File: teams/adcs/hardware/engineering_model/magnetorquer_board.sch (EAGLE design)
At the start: 35 parts

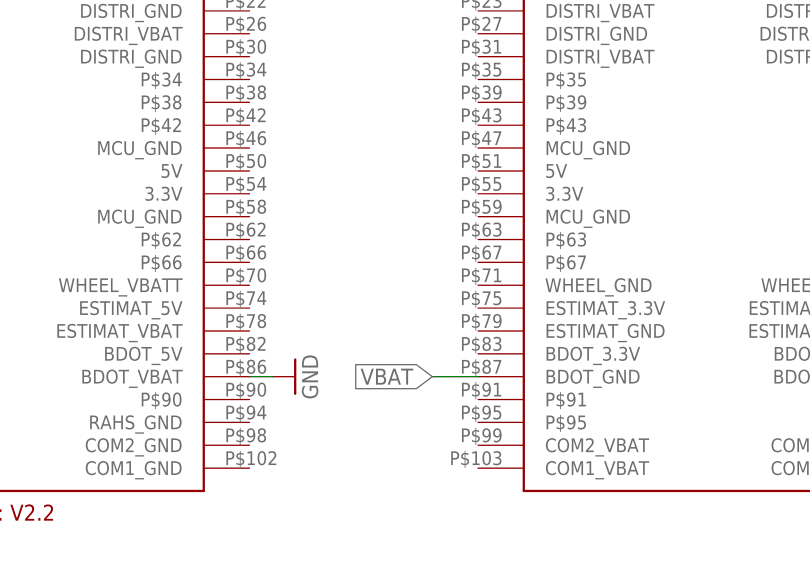
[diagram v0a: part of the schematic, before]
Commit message: ADCS/MT: Add capacitor to VBAT
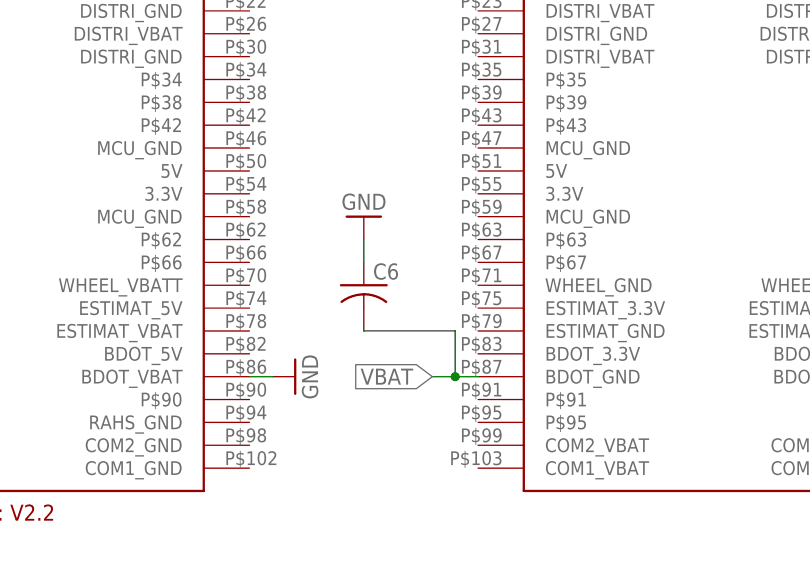
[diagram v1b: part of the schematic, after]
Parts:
- added C6: (no value), rcl:C-USC0805
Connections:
- net GND: now also C6.1
- net VBAT: now also C6.2
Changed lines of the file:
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@@
 <?xml version="1.0" encoding="utf-8"?>
 <!DOCTYPE eagle SYSTEM "eagle.dtd">
-<eagle version="8.3.2">
+<eagle version="8.4.0">
 <drawing>
 <settings>
@@
 <part name="R6" library="rcl" library_urn="urn:adsk.eagle:library:334" deviceset="R-US_" device="R0805" package3d_urn="urn:adsk.eagle:package:23553/2"/>
 <part name="GND21" library="supply1" library_urn="urn:adsk.eagle:library:371" deviceset="GND" device=""/>
+<part name="C6" library="rcl" library_urn="urn:adsk.eagle:library:334" deviceset="C-US" device="C0805" package3d_urn="urn:adsk.eagle:package:23617/2"/>
+<part name="GND23" library="supply1" library_urn="urn:adsk.eagle:library:371" deviceset="GND" device=""/>
 </parts>
 <sheets>
@@
 <instance part="R6" gate="G$1" x="58.42" y="147.32" rot="R90"/>
 <instance part="GND21" gate="1" x="58.42" y="139.7" rot="MR0"/>
+<instance part="C6" gate="G$1" x="43.18" y="43.18"/>
+<instance part="GND23" gate="1" x="43.18" y="50.8" rot="R180"/>
 </instances>
 <busses>
@@
 <pinref part="R6" gate="G$1" pin="1"/>
 <pinref part="GND21" gate="1" pin="GND"/>
+</segment>
+<segment>
+<pinref part="C6" gate="G$1" pin="1"/>
+<pinref part="GND23" gate="1" pin="GND"/>
+<wire x1="43.18" y1="45.72" x2="43.18" y2="48.26" width="0.1524" layer="91"/>
 </segment>
 </net>
@@
 <segment>
 <pinref part="U$1" gate="G$1" pin="BDOT_GND@87"/>
-<wire x1="55.88" y1="33.02" x2="50.8" y2="33.02" width="0.1524" layer="91"/>
+<wire x1="55.88" y1="33.02" x2="53.34" y2="33.02" width="0.1524" layer="91"/>
 <label x="50.8" y="33.02" size="1.778" layer="95" rot="R180" xref="yes"/>
-</segment>
-<segment>
+<pinref part="C6" gate="G$1" pin="2"/>
+<wire x1="53.34" y1="33.02" x2="50.8" y2="33.02" width="0.1524" layer="91"/>
+<wire x1="43.18" y1="38.1" x2="53.34" y2="38.1" width="0.1524" layer="91"/>
+<wire x1="53.34" y1="38.1" x2="53.34" y2="33.02" width="0.1524" layer="91"/>
+<junction x="53.34" y="33.02"/>
+</segment>
+<segment>

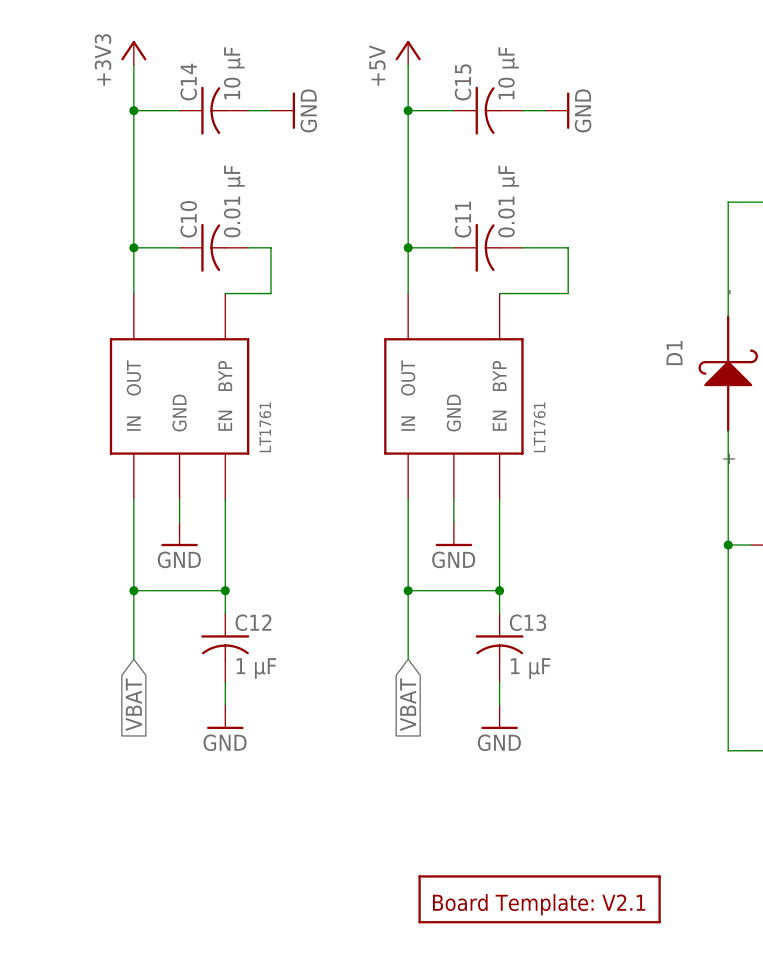
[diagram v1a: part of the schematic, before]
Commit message: ADCS/MT: Switched existing LDOs to LDOs from design blocks
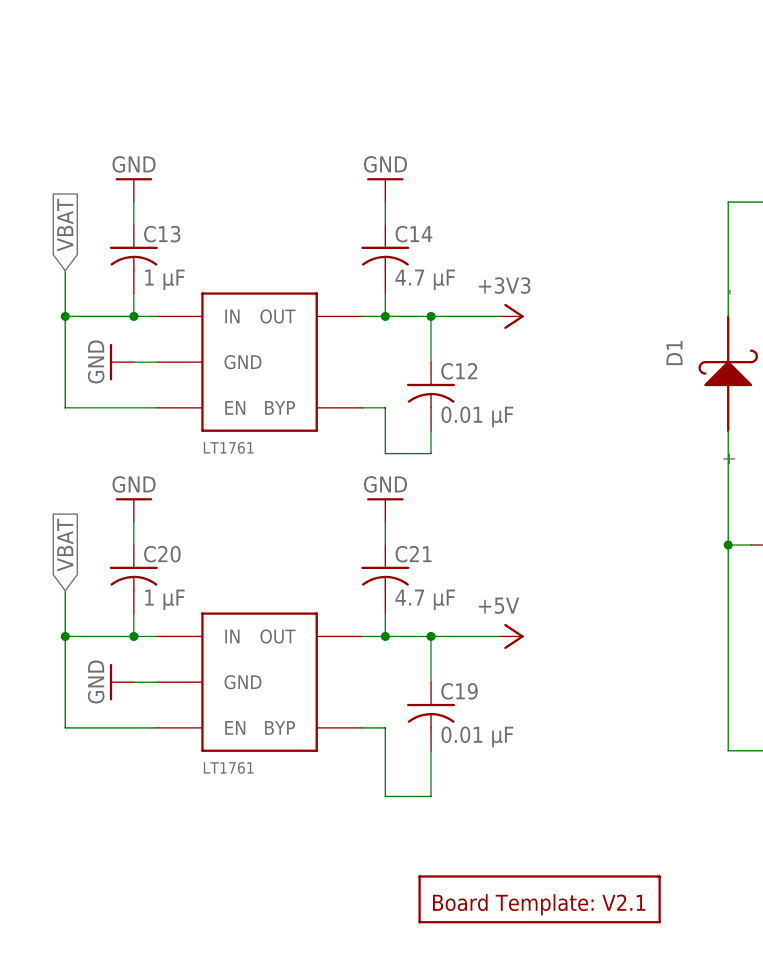
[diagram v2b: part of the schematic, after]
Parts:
- removed C10, C11: 0.01 μF, rcl:C-USC0805
- removed C15: 10 μF, rcl:C-USC0805
- removed LDO_3V3, LDO_5V: LINEAR_LDO_LT1761-X, DubSat1 Components:LINEAR_LDO_LT1761-X
- added C19: 0.01 μF, rcl:C-USC0805
- added C20: 1 μF, rcl:C-USC0805
- added C21: 4.7 μF, rcl:C-USC0805
- added LDO_3V1, LDO_5V1: LINEAR_LDO_LT1761-X, DubSat1 Components:LINEAR_LDO_LT1761-X
- C12: value 1 μF -> 0.01 μF
- C14: value 10 μF -> 4.7 μF
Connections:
- removed net N$26: C10.2, LDO_3V3.BYP
- removed net N$33: C11.2, LDO_5V.BYP
- new net N$4: C12.2, LDO_3V1.BYP
- new net N$8: C19.2, LDO_5V1.BYP
- net +3V3: now also C12.1, C14.2, LDO_3V1.OUT; no longer C10.1, C14.1, LDO_3V3.OUT
- net +5V: now also C19.1, C21.2, LDO_5V1.OUT; no longer C11.1, C15.1, LDO_5V.OUT
- net GND: now also C13.1, C14.1, C20.1, C21.1, LDO_3V1.GND, LDO_5V1.GND; no longer C12.2, C13.2, C14.2, C15.2, LDO_3V3.GND, LDO_5V.GND
- net VBAT: now also C13.2, C20.2, LDO_3V1.EN, LDO_3V1.IN, LDO_5V1.EN, LDO_5V1.IN; no longer C12.1, C13.1, LDO_3V3.EN, LDO_3V3.IN, LDO_5V.EN, LDO_5V.IN
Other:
- moved on the sheet: C12, C13, C14
